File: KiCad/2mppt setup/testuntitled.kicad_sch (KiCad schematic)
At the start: 3 parts, among them U1 BUCK_24V_5V_5A

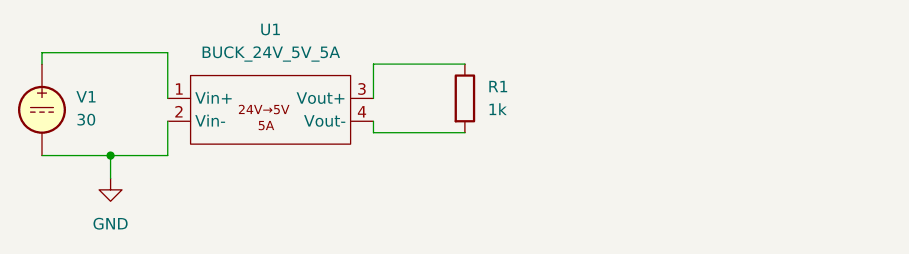
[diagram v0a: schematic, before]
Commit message: exclude text from sim
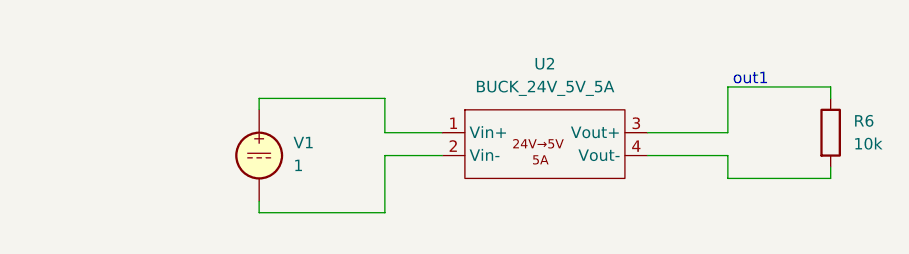
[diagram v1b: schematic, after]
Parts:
- removed R1: 1k, symbol Device:R
- removed U1: BUCK_24V_5V_5A, symbol Proa:BUCK_24V_5V_5A
- added R6: 10k, symbol Device:R
- added U2: BUCK_24V_5V_5A, symbol Proa:BUCK_24V_5V_5A
- V1: value 30 -> 1
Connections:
- net at V1.1: now also U2.1 (Vin+)
- net GND: no longer names the net of V1.2
- net GND: now also U2.2 (Vin-)
- new net: R6.1, U2.3 (Vout+)
- new net: R6.2, U2.4 (Vout-)
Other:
- note added: "out1"
